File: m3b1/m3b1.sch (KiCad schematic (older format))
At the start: 26 parts, among them P5 MicroD-37Pins, Q1 MD3251, Q2 MD3251, U1 MC307, U10 MC309, U11 MC309, U12 MC310, U13 MC309, U2 MC306, U3 MC306, U4 MC306, U5 MC302, U6 MC306, U7 MC306, U8 MC301, U9 MC301

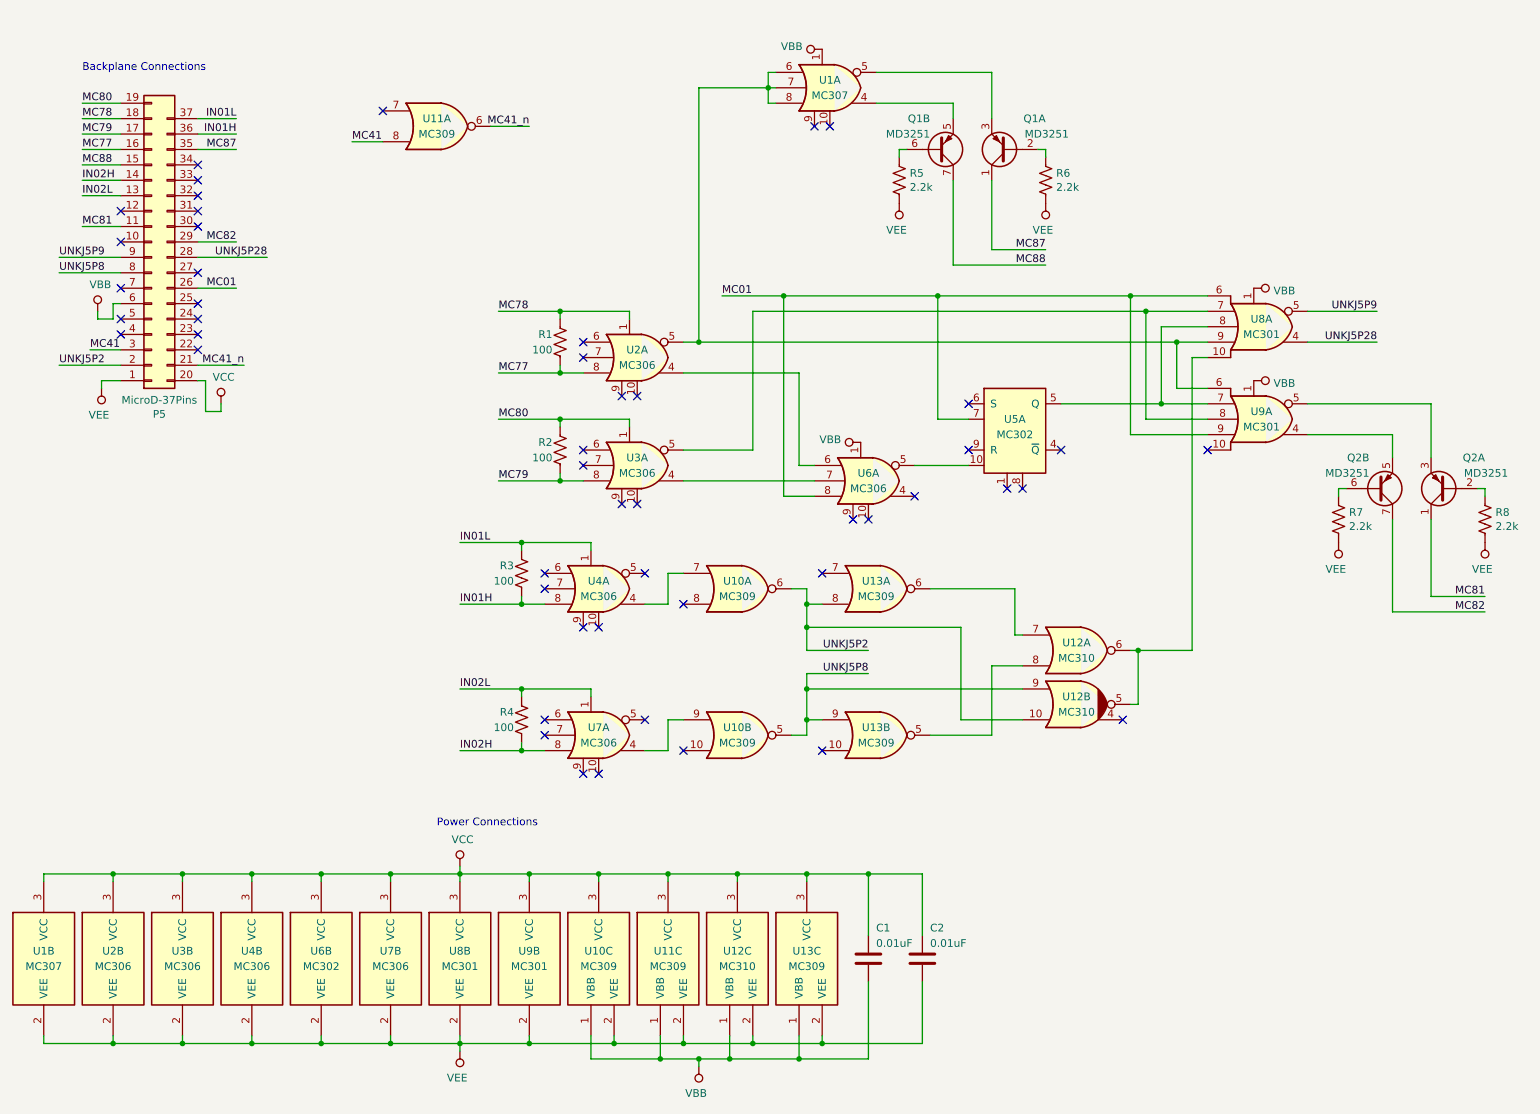
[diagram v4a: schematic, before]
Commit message: Finished untangling the module 3 schematics and gave every net a name
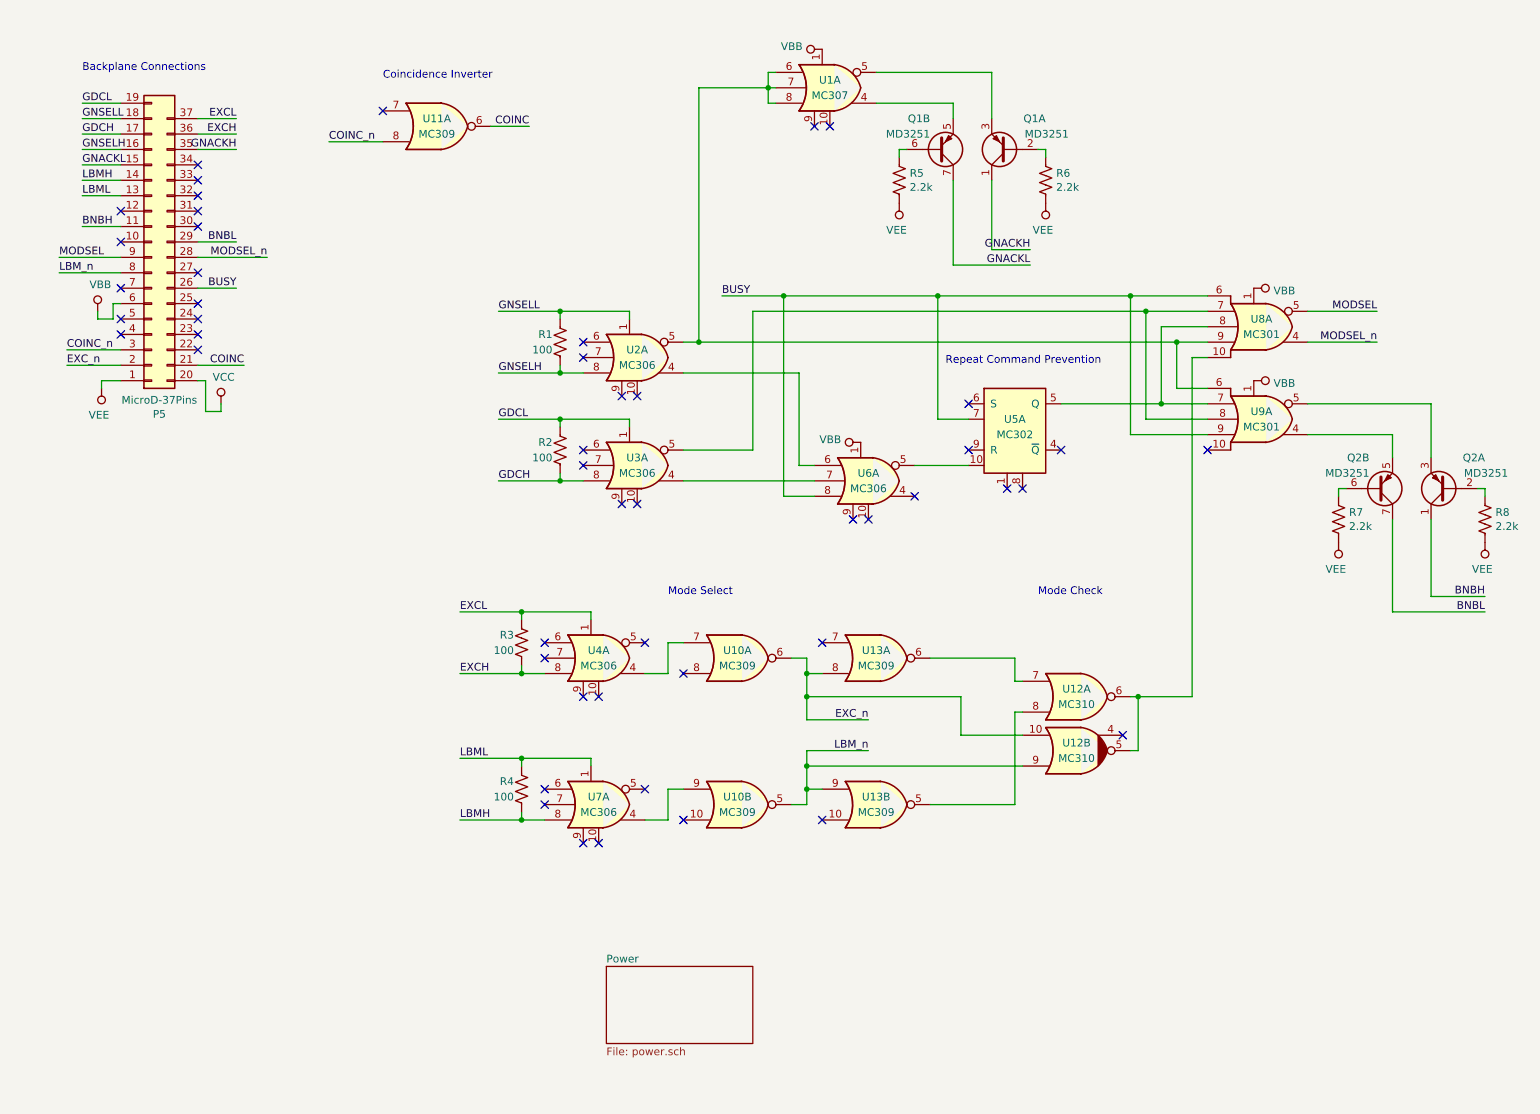
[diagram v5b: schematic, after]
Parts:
- removed C1, C2: 0.01uF, symbol Device:C
- removed unit 2 of U1
- removed unit 3 of U10
- removed unit 3 of U11
- removed unit 3 of U12
- removed unit 3 of U13
- removed unit 2 of U2
- removed unit 2 of U3
- removed unit 2 of U4
- removed unit 2 of U6
- removed unit 2 of U7
- removed unit 2 of U8
- removed unit 2 of U9
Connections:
- net IN01H renamed EXCH
- net IN01L renamed EXCL
- net IN02H renamed LBMH
- net IN02L renamed LBML
- net MC01 renamed BUSY
- net MC41 renamed COINC_n
- net MC41_n renamed COINC
- net MC77 renamed GNSELH
- net MC78 renamed GNSELL
- net MC79 renamed GDCH
- net MC80 renamed GDCL
- net MC81 renamed BNBH
- net MC82 renamed BNBL
- net MC87 renamed GNACKH
- net MC88 renamed GNACKL
- net UNKJ5P2 renamed EXC_n
- net UNKJ5P28 renamed MODSEL_n
- net UNKJ5P8 renamed LBM_n
- net UNKJ5P9 renamed MODSEL
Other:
- note added: "Coincidence Inverter"
- note added: "Mode Check"
- note added: "Mode Select"
- note added: "Repeat Command Prevention"
- note removed: "Power Connections"
- moved on the sheet: R3, R4, U10A, U10B, U12A, U12B, U13A, U13B, U4A, U7A

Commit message: Greatly cleaned up all of the schematics so far; everything passes DRC.
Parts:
- added C1, C2: 0.1uF, symbol Device:C
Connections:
- net VBB: now also C1.2
- net VCC: now also C1.1, C2.1
- net VEE: now also C2.2
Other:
- note added: "Buffer Not Busy"
- note added: "Execute"
- note added: "G&N Select"
- note added: "Group Decode Check"
- note added: "Load Buffer Memory"
- note added: "Selection Acknowledgment"
